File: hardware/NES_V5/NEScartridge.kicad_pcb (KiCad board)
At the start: 4 copper layers, 90 x 144.2 mm, 39 parts, among them J1 Conn_02x36_Top_Bottom, U1 TXS0108EPW, U10 TXS0108EPW, U11 TXS0108EPW, U2 TXS0108EPW, U5 TXS0108EPW, U6 TXS0108EPW, U7 TXS0108EPW, U8 TXS0108EPW, U9 TXS0108EPW

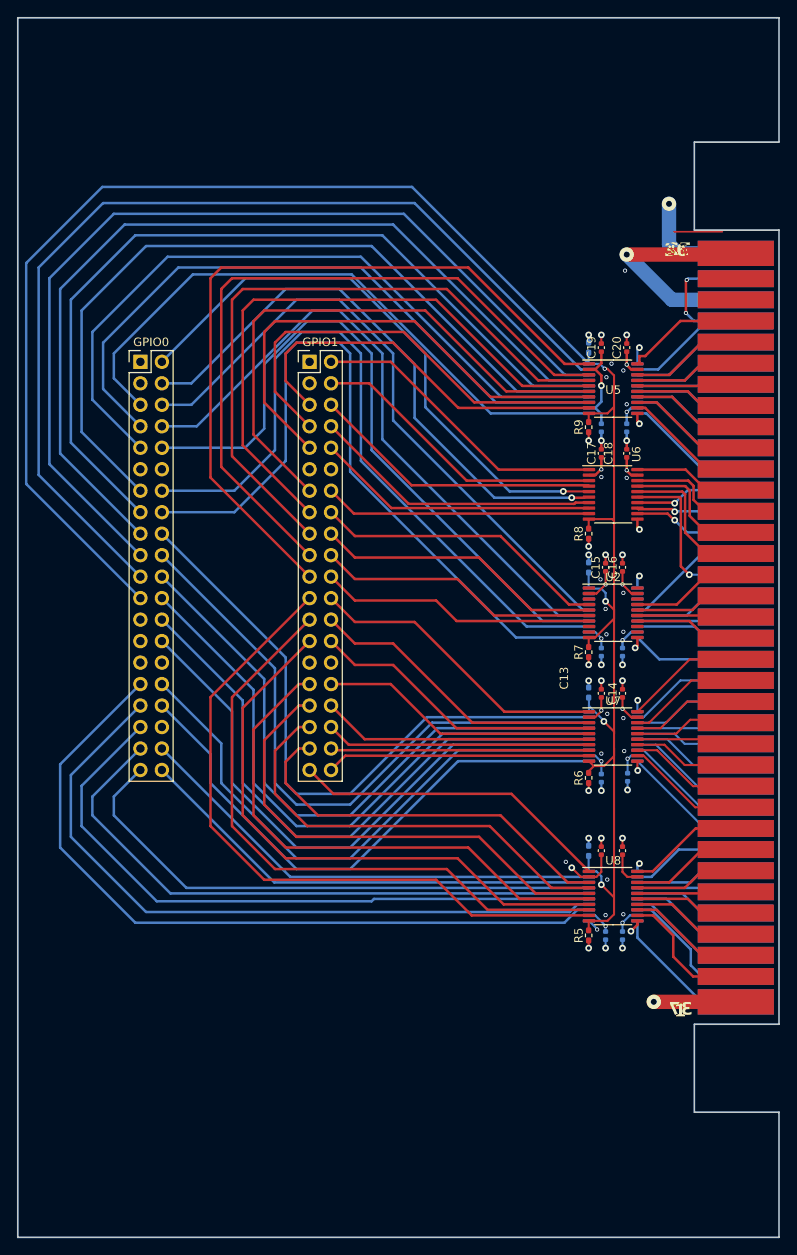
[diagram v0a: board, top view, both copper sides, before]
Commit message: Corrected DRC errors/warning on V5
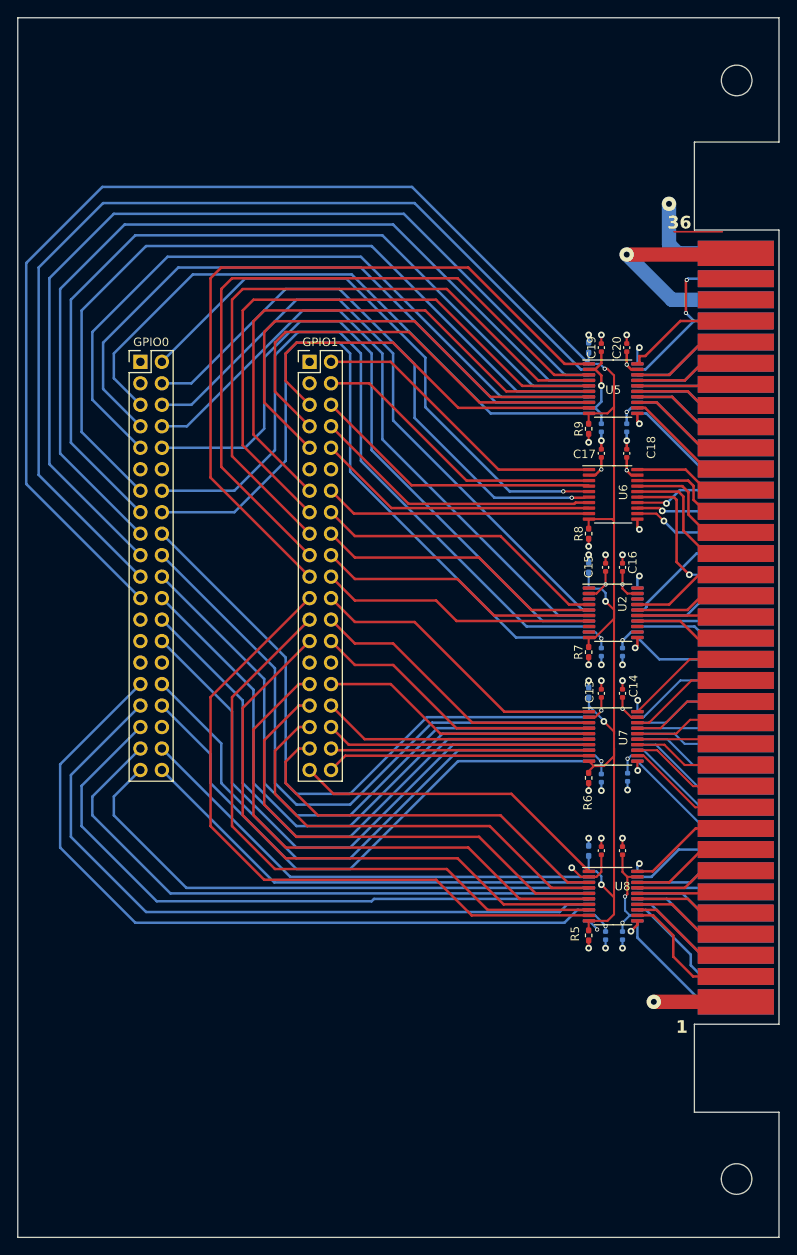
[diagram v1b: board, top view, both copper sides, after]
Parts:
- moved R9 0.20 mm to (142.5, 68.6)
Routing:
- net +5V: track 171.9 -> 177.1 mm, vias 9 -> 10
- net (69)PPUD4: track 30.1 -> 25.2 mm
- net (22C)CIRAMA10: track 68.6 -> 68.0 mm
- net GND: track 62.3 -> 62.5 mm, vias 56 -> 36
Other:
- outline, holes or cut-outs redrawn
- board text removed: "37"
- board text removed: "72"
